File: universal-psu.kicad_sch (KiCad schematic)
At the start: 4 parts, among them J1 Conn_Receptacle_2P, J2 Screw_Terminal_01x04, J3 Screw_Terminal_01x04

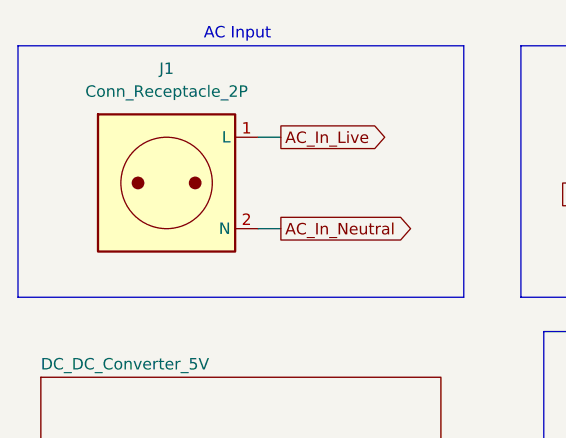
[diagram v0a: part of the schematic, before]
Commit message: Layout import and schema fixes.
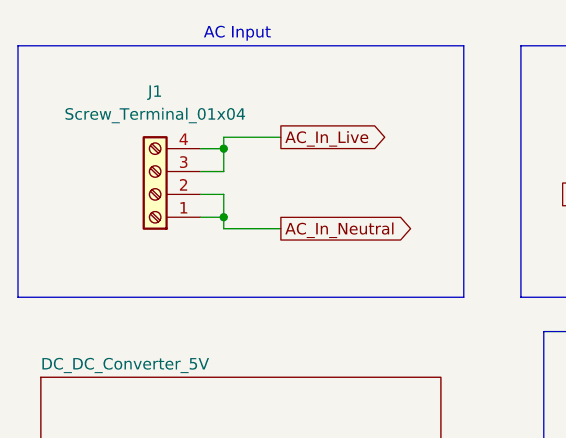
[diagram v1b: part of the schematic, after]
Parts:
- removed J1: Conn_Receptacle_2P, TerminalBlock_Phoenix:TerminalBlock_Phoenix_PT-1,5-2-3.5-H_1x02_P3.50mm_Horizontal, symbol Connector:Conn_Receptacle_2P
- added J1: Screw_Terminal_01x04, TerminalBlock_Phoenix:TerminalBlock_Phoenix_MKDS-1,5-4-5.08_1x04_P5.08mm_Horizontal, symbol Connector:Screw_Terminal_01x04
- J2, J3: footprint TerminalBlock_Phoenix:TerminalBlock_Phoenix_PT-1,5-4-3.5-H_1x04_P3.50mm_Horizontal -> TerminalBlock_Phoenix:TerminalBlock_Phoenix_MKDS-1,5-4-5.08_1x04_P5.08mm_Horizontal; MANUFACTURER (none) -> Phoenix Contact; Manufacturer Part Number (none) -> 1715048; Price (none) -> 257; Vendor Link (none) -> https://www.digikey.in/en/products/detail/phoenix-contact/1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; Vendor Part Number (none) -> 277-1260-ND
- PS1: MANUFACTURER (none) -> MEAN WELL USA Inc.; Manufacturer Part Number (none) -> IRM-60-12; Price (none) -> 1327; Vendor Link (none) -> https://www.digikey.in/en/products/detail/mean-well-usa-inc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; Vendor Part Number (none) -> 1866-3063-ND
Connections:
- net AC_In_Live: now also J1.3 (Pin_3), J1.4 (Pin_4)
- net AC_In_Neutral: now also J1.1 (Pin_1), J1.2 (Pin_2)

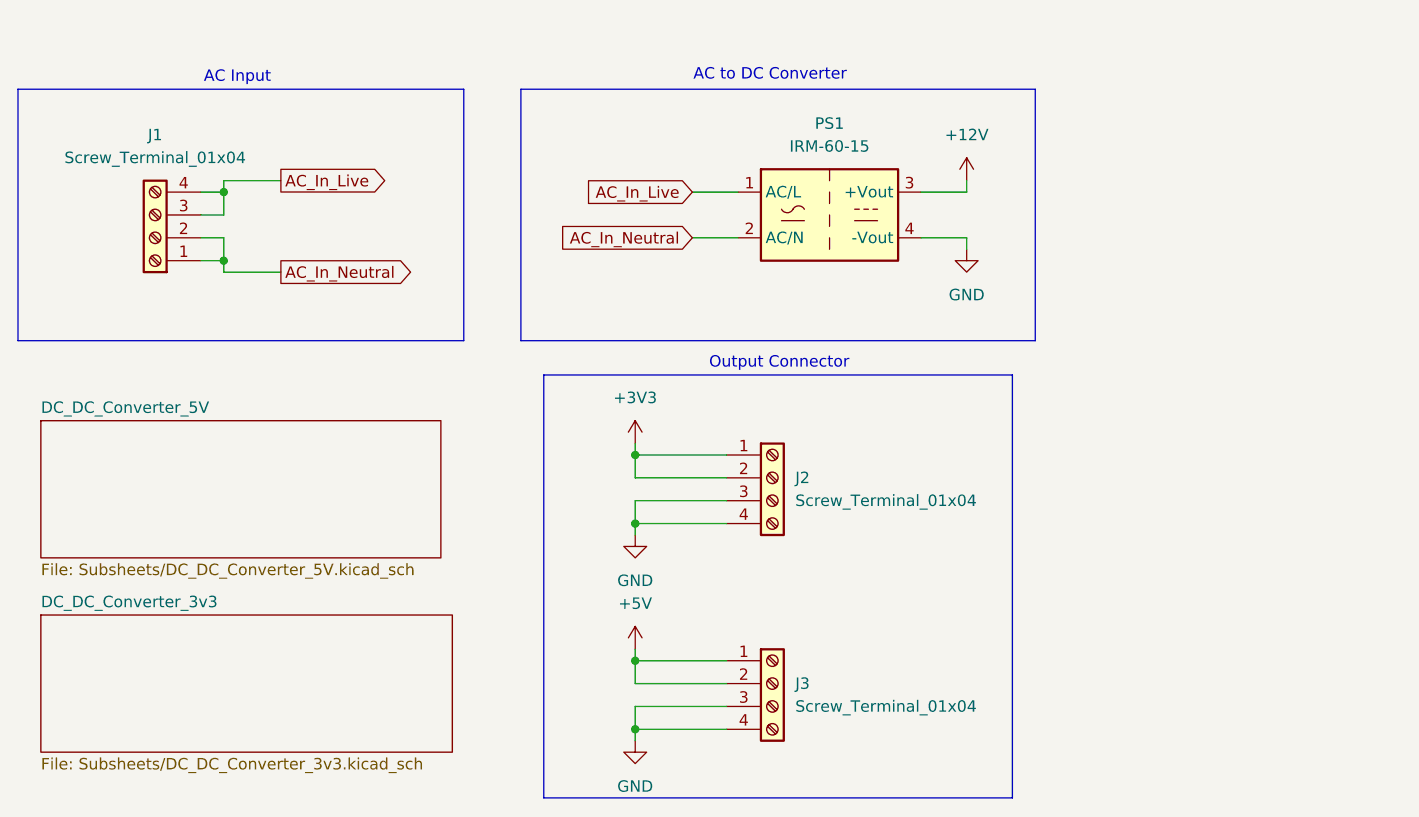
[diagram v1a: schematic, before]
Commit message: Layout  closed, some DRC  conflicts remain.
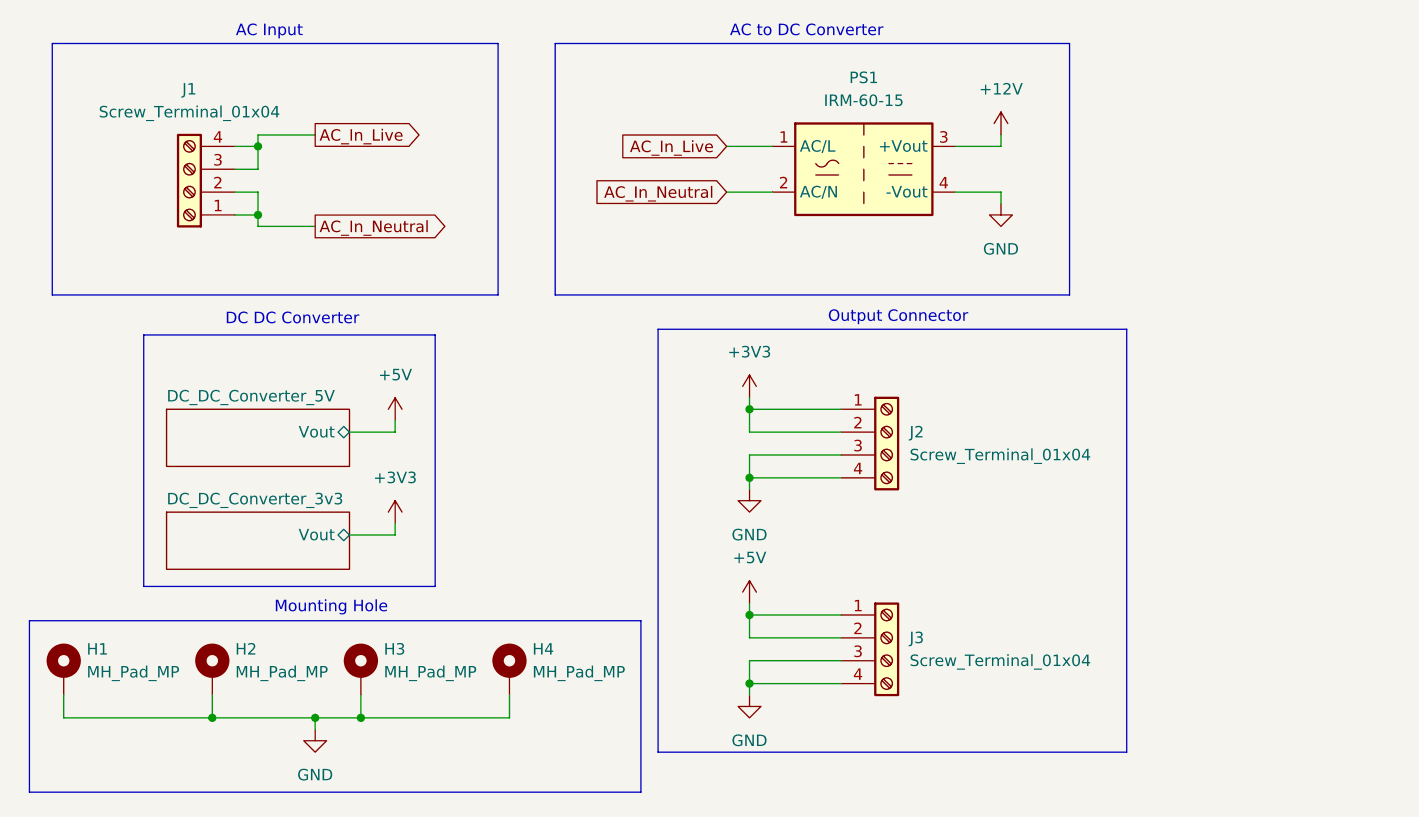
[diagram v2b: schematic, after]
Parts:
- added H1, H2, H3, H4: MH_Pad_MP, MountingHole:MountingHole_2.2mm_M2, symbol Mechanical:MountingHole_Pad_MP
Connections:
- net GND: now also H1.MP, H2.MP, H3.MP, H4.MP
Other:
- sheet DC_DC_Converter_3v3: file Subsheets/DC_DC_Converter_3v3.kicad_sch -> Subsheets/DC_DC_Converter_5V.kicad_sch
- sheet DC_DC_Converter_3v3 ports: added Vout; removed none
- sheet DC_DC_Converter_5V ports: added Vout; removed none
- note added: "DC DC Converter"
- note added: "Mounting Hole"
- moved on the sheet: J1, J2, J3, PS1

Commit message: Connector change and silkscreen
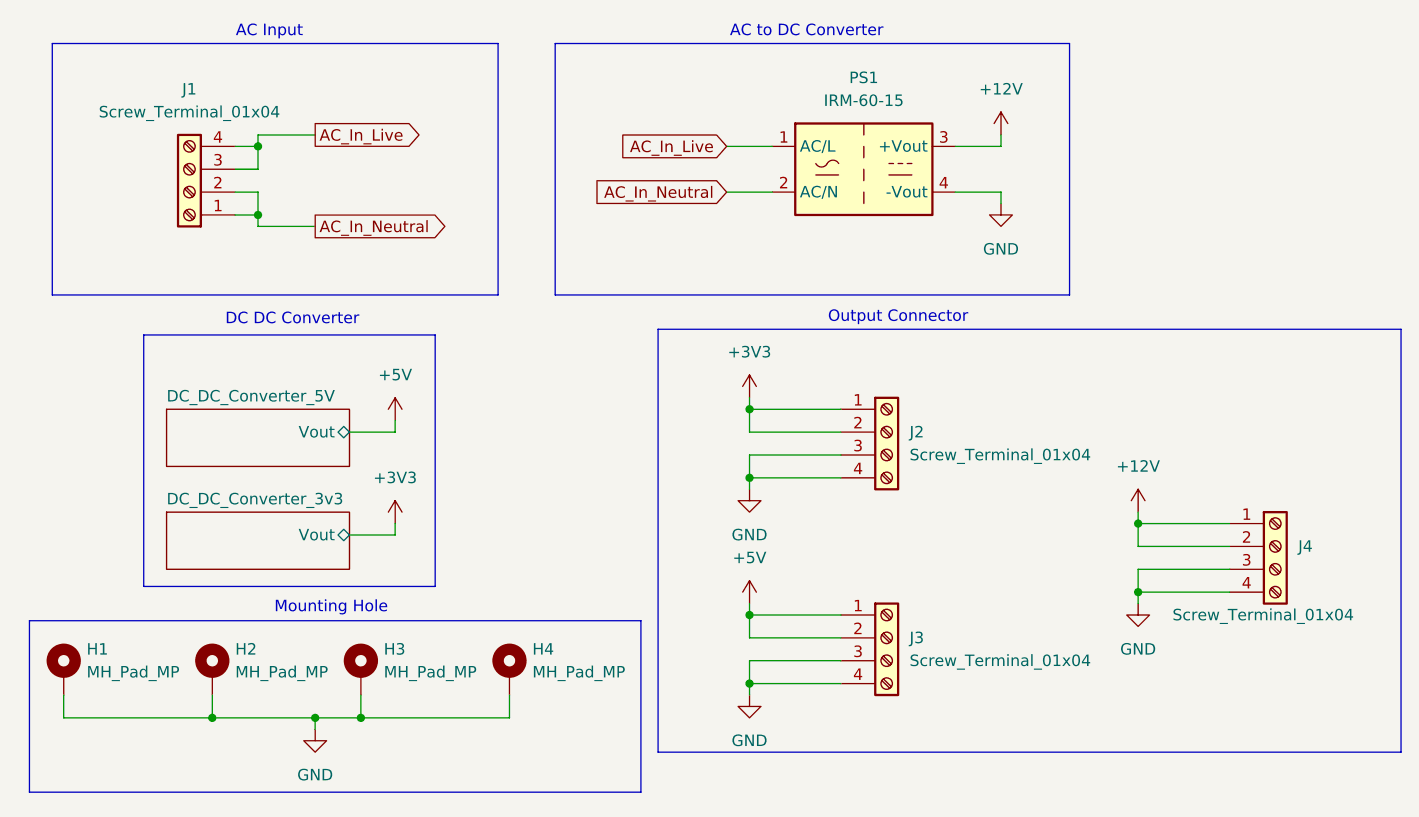
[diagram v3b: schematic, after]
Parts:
- added J4: Screw_Terminal_01x04, TerminalBlock_Phoenix:TerminalBlock_Phoenix_MKDS-1,5-4-5.08_1x04_P5.08mm_Horizontal, symbol Connector:Screw_Terminal_01x04
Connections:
- net +12V: now also J4.1 (Pin_1), J4.2 (Pin_2)
- net GND: now also J4.3 (Pin_3), J4.4 (Pin_4)
